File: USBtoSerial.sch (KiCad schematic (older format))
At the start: 8 parts, among them J7 USB_B_Micro, U3 FT231XS

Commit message: change USB to Serial chip, support charging
* exchanges FTDI FT231X for SILabs CP2102N
* adds MicroChip MCP73123 for LiFePO4 charging
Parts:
- removed C10: 100nF, Capacitor_SMD:C_0805_2012Metric, symbol Device:C
- added C?: 4.7μF, Capacitor_SMD:C_0805_2012Metric, symbol Device:C
- added D?: TX, symbol Device:LED
- added D?: RX, symbol Device:LED
- added R?: 47k5, symbol Device:R
- added R?: 22k1, symbol Device:R
- added R?: 1k, symbol Device:R
- added R? (x2): R, symbol Device:R
- C7: value 10nF -> 100nF
- U3: value FT231XS -> CP2102N-A01-GQFN28; footprint Package_SO:QSOP-20_3.9x8.7mm_P0.635mm -> Package_DFN_QFN:QFN-28-1EP_5x5mm_P0.5mm_EP3.35x3.35mm; symbol Interface_USB:FT231XS -> Interface_USB:CP2102N-A01-GQFN28
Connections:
- net labels added: CHR0, CHR1, CHREN, GPIO4, GPIO5, GPIO6, RS485_GPIO2, SUSPEND, VDD, ~CTS, ~DCD, ~DSR, ~DTR, ~RI, ~RSTb, ~RTS, ~RXT, ~SUSPENDb, ~TXT, ~WAKEUP_GPIO3
- net labels removed: CBUS0, CBUS1, CBUS2, CBUS3, CTS, DCD, DSR, DTR, RI, RTS
- wire segments 51 -> 70
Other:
- moved on the sheet: C8, C9, J7, R19, R20

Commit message: update drawing to 882a528a10f6fb48f6454efd446c1280f51ad1f8
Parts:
- D2, D3: renamed from D?; footprint (none) -> LED_SMD:LED_0805_2012Metric
- R26, R27, R28, R29, R30: renamed from R?; footprint (none) -> Resistor_SMD:R_0805_2012Metric
- gave numbers to parts that had none: 1
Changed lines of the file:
@@
 	6900 3450 7100 3450
 $Comp
-L Device:R R?
+L Device:R R28
 U 1 1 5EF23249
 P 5150 2450
-F 0 "R?" H 5220 2496 50  0000 L CNN
+F 0 "R28" H 5220 2496 50  0000 L CNN
 F 1 "47k5" H 5220 2405 50  0000 L CNN
-F 2 "" V 5080 2450 50  0001 C CNN
+F 2 "Resistor_SMD:R_0805_2012Metric" V 5080 2450 50  0001 C CNN
 F 3 "~" H 5150 2450 50  0001 C CNN
 	1    5150 2450
@@
 $EndComp
 $Comp
-L Device:R R?
+L Device:R R27
 U 1 1 5EF23E1A
 P 5150 1850
-F 0 "R?" H 5220 1896 50  0000 L CNN
+F 0 "R27" H 5220 1896 50  0000 L CNN
 F 1 "22k1" H 5220 1805 50  0000 L CNN
-F 2 "" V 5080 1850 50  0001 C CNN
+F 2 "Resistor_SMD:R_0805_2012Metric" V 5080 1850 50  0001 C CNN
 F 3 "~" H 5150 1850 50  0001 C CNN
 	1    5150 1850
@@
 P 5150 2800
 AR Path="/5EF27218" Ref="#PWR?"  Part="1"
-AR Path="/5EFCE977/5EF27218" Ref="#PWR?"  Part="1"
-F 0 "#PWR?" H 5150 2550 50  0001 C CNN
+AR Path="/5EFCE977/5EF27218" Ref="#PWR0108"  Part="1"
+F 0 "#PWR0108" H 5150 2550 50  0001 C CNN
 F 1 "GND" H 5155 2627 50  0000 C CNN
 F 2 "" H 5150 2800 50  0001 C CNN
@@
 	5150 1500 5150 1700
 $Comp
-L Device:R R?
+L Device:R R26
 U 1 1 5EF2AEF8
 P 5800 1600
-F 0 "R?" H 5870 1646 50  0000 L CNN
+F 0 "R26" H 5870 1646 50  0000 L CNN
 F 1 "1k" H 5870 1555 50  0000 L CNN
-F 2 "" V 5730 1600 50  0001 C CNN
+F 2 "Resistor_SMD:R_0805_2012Metric" V 5730 1600 50  0001 C CNN
 F 3 "~" H 5800 1600 50  0001 C CNN
 	1    5800 1600
@@
 P 6300 1050
 AR Path="/5EF2E274" Ref="#PWR?"  Part="1"
-AR Path="/5EFCE977/5EF2E274" Ref="#PWR?"  Part="1"
-F 0 "#PWR?" H 6300 900 50  0001 C CNN
+AR Path="/5EFCE977/5EF2E274" Ref="#PWR0109"  Part="1"
+F 0 "#PWR0109" H 6300 900 50  0001 C CNN
 F 1 "VBUS" H 6315 1223 50  0000 C CNN
 F 2 "" H 6300 1050 50  0001 C CNN
@@
 P 1450 1850
 AR Path="/5EF314AF" Ref="C?"  Part="1"
-AR Path="/5EFCE977/5EF314AF" Ref="C?"  Part="1"
-F 0 "C?" H 1565 1896 50  0000 L CNN
+AR Path="/5EFCE977/5EF314AF" Ref="C6"  Part="1"
+F 0 "C6" H 1565 1896 50  0000 L CNN
 F 1 "4.7μF" H 1565 1805 50  0000 L CNN
 F 2 "Capacitor_SMD:C_0805_2012Metric" H 1488 1700 50  0001 C CNN
@@
 P 1450 1600
 AR Path="/5EF314B9" Ref="#PWR?"  Part="1"
-AR Path="/5EFCE977/5EF314B9" Ref="#PWR?"  Part="1"
-F 0 "#PWR?" H 1450 1450 50  0001 C CNN
+AR Path="/5EFCE977/5EF314B9" Ref="#PWR0110"  Part="1"
+F 0 "#PWR0110" H 1450 1450 50  0001 C CNN
 F 1 "VBUS" H 1465 1773 50  0000 C CNN
 F 2 "" H 1450 1600 50  0001 C CNN
@@
 P 1450 2100
 AR Path="/5EF314C3" Ref="#PWR?"  Part="1"
-AR Path="/5EFCE977/5EF314C3" Ref="#PWR?"  Part="1"
-F 0 "#PWR?" H 1450 1850 50  0001 C CNN
+AR Path="/5EFCE977/5EF314C3" Ref="#PWR0111"  Part="1"
+F 0 "#PWR0111" H 1450 1850 50  0001 C CNN
 F 1 "GND" H 1455 1927 50  0000 C CNN
 F 2 "" H 1450 2100 50  0001 C CNN
@@
 	6900 2750 7100 2750
 $Comp
-L Device:LED D?
+L Device:LED D2
 U 1 1 5EF67E52
 P 1450 3050
-F 0 "D?" H 1443 3267 50  0000 C CNN
+F 0 "D2" H 1443 3267 50  0000 C CNN
 F 1 "TX" H 1443 3176 50  0000 C CNN
-F 2 "" H 1450 3050 50  0001 C CNN
+F 2 "LED_SMD:LED_0805_2012Metric" H 1450 3050 50  0001 C CNN
 F 3 "~" H 1450 3050 50  0001 C CNN
 	1    1450 3050
@@
 ~TXT
 $Comp
-L Device:LED D?
+L Device:LED D3
 U 1 1 5EF69A52
 P 1450 3300
-F 0 "D?" H 1443 3137 50  0000 C CNN
+F 0 "D3" H 1443 3137 50  0000 C CNN
 F 1 "RX" H 1443 3046 50  0000 C CNN
-F 2 "" H 1450 3300 50  0001 C CNN
+F 2 "LED_SMD:LED_0805_2012Metric" H 1450 3300 50  0001 C CNN
 F 3 "~" H 1450 3300 50  0001 C CNN
 	1    1450 3300
@@
 	1150 3300 1300 3300
 $Comp
-L Device:R R?
+L Device:R R29
 U 1 1 5EF6C431
 P 1900 3050
-F 0 "R?" V 1693 3050 50  0000 C CNN
+F 0 "R29" V 1693 3050 50  0000 C CNN
 F 1 "R" V 1784 3050 50  0000 C CNN
-F 2 "" V 1830 3050 50  0001 C CNN
+F 2 "Resistor_SMD:R_0805_2012Metric" V 1830 3050 50  0001 C CNN
 F 3 "~" H 1900 3050 50  0001 C CNN
 	1    1900 3050
@@
 $EndComp
 $Comp
-L Device:R R?
+L Device:R R30
 U 1 1 5EF6CF1D
 P 1900 3300
-F 0 "R?" V 2015 3300 50  0000 C CNN
+F 0 "R30" V 2015 3300 50  0000 C CNN
 F 1 "R" V 2106 3300 50  0000 C CNN
-F 2 "" V 1830 3300 50  0001 C CNN
+F 2 "Resistor_SMD:R_0805_2012Metric" V 1830 3300 50  0001 C CNN
 F 3 "~" H 1900 3300 50  0001 C CNN
 	1    1900 3300

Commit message: Add JCLPCB/LCSC part numbers
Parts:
- C6: LCSC (none) -> C1779
- C7: LCSC (none) -> C49678
- C8, C9: LCSC (none) -> C14857
- D2: LCSC (none) -> C84256
- D3: LCSC (none) -> C2297
- R19, R20: LCSC (none) -> C17594
- R26: LCSC (none) -> C17513
- R27: LCSC (none) -> C17518
- R28: LCSC (none) -> C26011
- R29, R30: LCSC (none) -> C17630
- U3: LCSC (none) -> C105167
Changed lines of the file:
@@
 EESchema Schematic File Version 4
+LIBS:ULPSoilMonitor-cache
 EELAYER 30 0
 EELAYER END
@@
 F 2 "Resistor_SMD:R_0805_2012Metric" V 3930 1900 50  0001 C CNN
 F 3 "~" H 4000 1900 50  0001 C CNN
+F 4 "C17594" H 4000 1900 50  0001 C CNN "LCSC"
 	1    4000 1900
 	0    1    1    0
@@
 F 2 "Resistor_SMD:R_0805_2012Metric" V 3930 1800 50  0001 C CNN
 F 3 "~" H 4000 1800 50  0001 C CNN
+F 4 "C17594" H 4000 1800 50  0001 C CNN "LCSC"
 	1    4000 1800
 	0    -1   -1   0
@@
 F 2 "Capacitor_SMD:C_0805_2012Metric" H 3688 2100 50  0001 C CNN
 F 3 "~" H 3650 2250 50  0001 C CNN
+F 4 "C14857" H 3650 2250 50  0001 C CNN "LCSC"
 	1    3650 2250
 	1    0    0    -1
@@
 F 2 "Capacitor_SMD:C_0805_2012Metric" H 3388 2100 50  0001 C CNN
 F 3 "~" H 3350 2250 50  0001 C CNN
+F 4 "C14857" H 3350 2250 50  0001 C CNN "LCSC"
 	1    3350 2250
 	1    0    0    -1
@@
 F 2 "Capacitor_SMD:C_0805_2012Metric" H 1938 1700 50  0001 C CNN
 F 3 "~" H 1900 1850 50  0001 C CNN
+F 4 "C49678" H 1900 1850 50  0001 C CNN "LCSC"
 	1    1900 1850
 	1    0    0    -1
@@
 F 2 "Package_DFN_QFN:QFN-28-1EP_5x5mm_P0.5mm_EP3.35x3.35mm" H 6850 1650 50  0001 L CNN
 F 3 "https://www.silabs.com/documents/public/data-sheets/cp2102n-datasheet.pdf" H 6450 2100 50  0001 C CNN
+F 4 "C105167" H 6400 2850 50  0001 C CNN "LCSC"
 	1    6400 2850
 	1    0    0    -1
@@
 F 2 "Resistor_SMD:R_0805_2012Metric" V 5080 2450 50  0001 C CNN
 F 3 "~" H 5150 2450 50  0001 C CNN
+F 4 "C26011" H 5150 2450 50  0001 C CNN "LCSC"
 	1    5150 2450
 	1    0    0    -1
@@
 F 2 "Resistor_SMD:R_0805_2012Metric" V 5080 1850 50  0001 C CNN
 F 3 "~" H 5150 1850 50  0001 C CNN
+F 4 "C17518" H 5150 1850 50  0001 C CNN "LCSC"
 	1    5150 1850
 	1    0    0    -1
@@
 F 2 "Resistor_SMD:R_0805_2012Metric" V 5730 1600 50  0001 C CNN
 F 3 "~" H 5800 1600 50  0001 C CNN
+F 4 "C17513" H 5800 1600 50  0001 C CNN "LCSC"
 	1    5800 1600
 	1    0    0    -1
@@
 F 2 "Capacitor_SMD:C_0805_2012Metric" H 1488 1700 50  0001 C CNN
 F 3 "~" H 1450 1850 50  0001 C CNN
+F 4 "C1779" H 1450 1850 50  0001 C CNN "LCSC"
 	1    1450 1850
 	1    0    0    -1
@@
 F 2 "LED_SMD:LED_0805_2012Metric" H 1450 3050 50  0001 C CNN
 F 3 "~" H 1450 3050 50  0001 C CNN
+F 4 "C84256" H 1450 3050 50  0001 C CNN "LCSC"
 	1    1450 3050
 	1    0    0    -1
@@
 F 2 "LED_SMD:LED_0805_2012Metric" H 1450 3300 50  0001 C CNN
 F 3 "~" H 1450 3300 50  0001 C CNN
+F 4 "C2297" H 1450 3300 50  0001 C CNN "LCSC"
 	1    1450 3300
 	1    0    0    -1
@@
 F 2 "Resistor_SMD:R_0805_2012Metric" V 1830 3050 50  0001 C CNN
 F 3 "~" H 1900 3050 50  0001 C CNN
+F 4 "C17630" H 1900 3050 50  0001 C CNN "LCSC"
 	1    1900 3050
 	0    1    1    0
@@
 F 2 "Resistor_SMD:R_0805_2012Metric" V 1830 3300 50  0001 C CNN
 F 3 "~" H 1900 3300 50  0001 C CNN
+F 4 "C17630" H 1900 3300 50  0001 C CNN "LCSC"
 	1    1900 3300
 	0    1    1    0

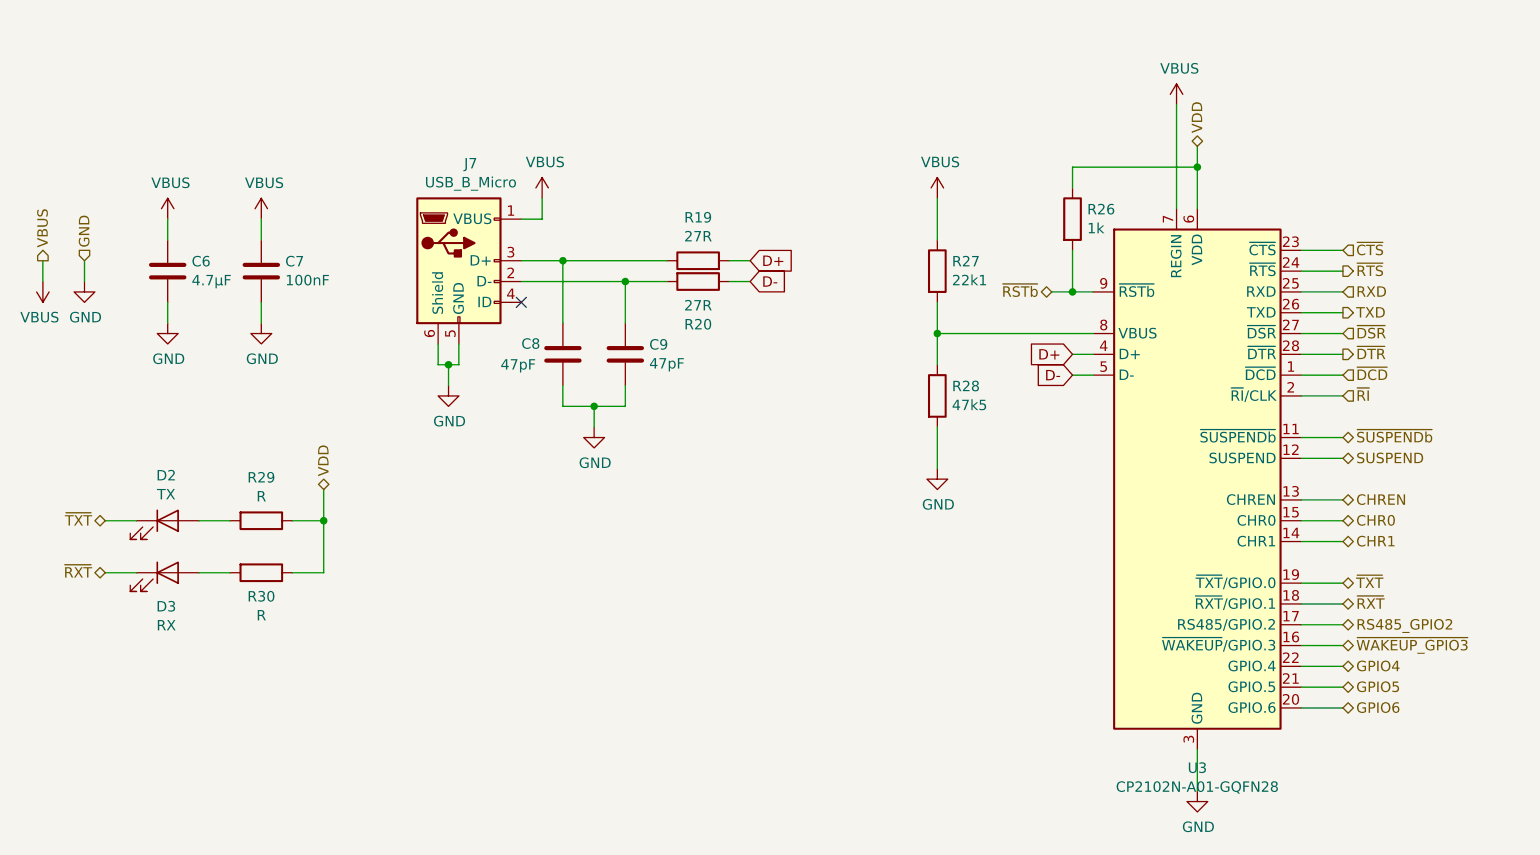
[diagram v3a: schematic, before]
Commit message: Set USB-serial DNP
Disable USB-serial
Add switches for LiFePo charger PROG setting
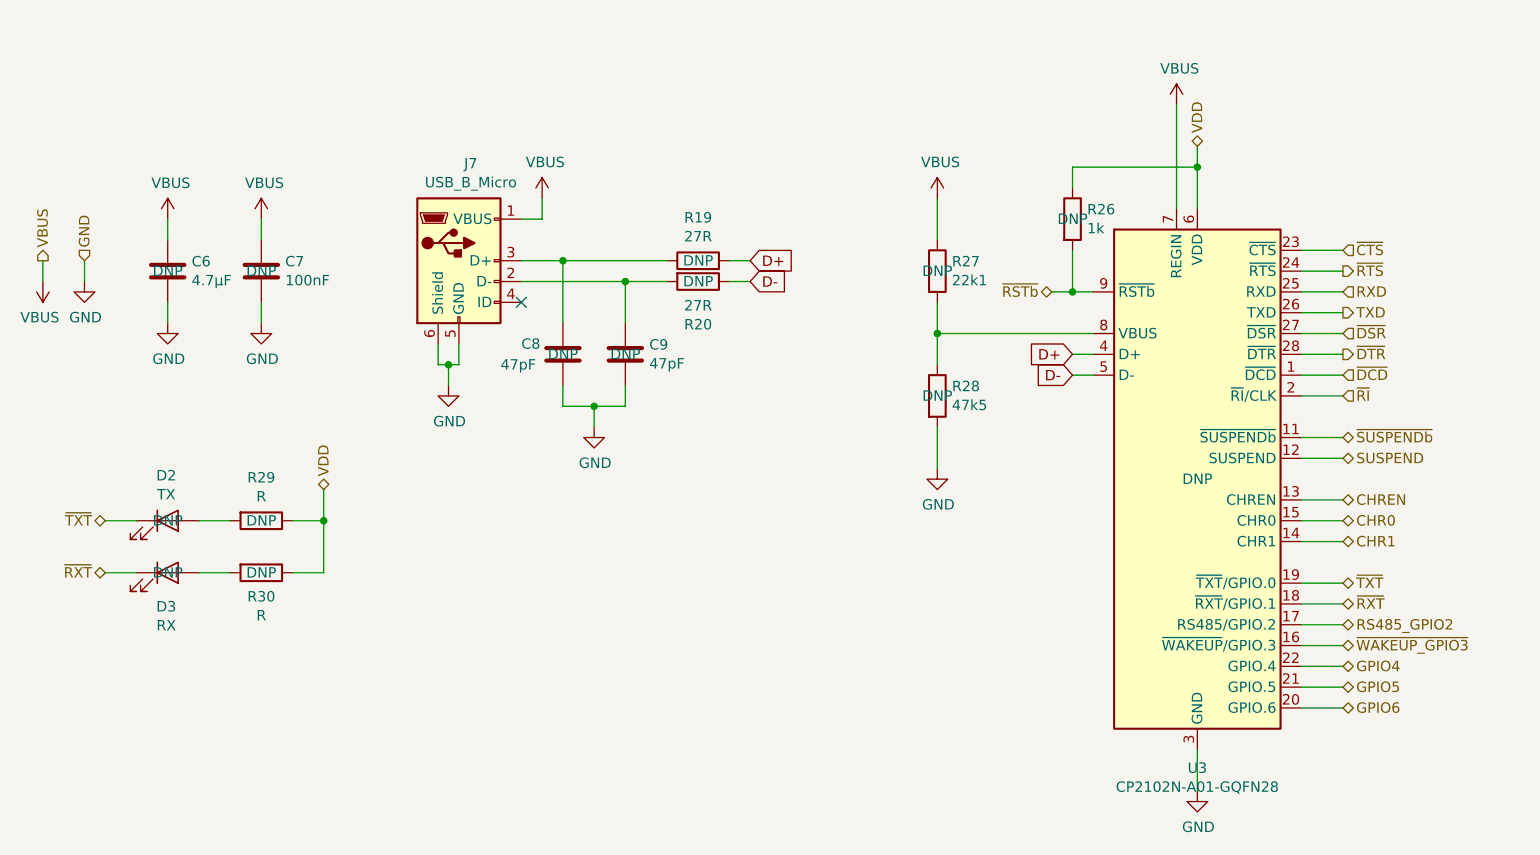
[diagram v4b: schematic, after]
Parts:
- C6, C7, C8, C9, D2, D3, R19, R20, R26, R27, R28, R29, R30, U3: DNP (none) -> DNP
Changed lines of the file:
@@
 F 3 "~" H 4000 1900 50  0001 C CNN
 F 4 "C17594" H 4000 1900 50  0001 C CNN "LCSC"
+F 5 "DNP" V 4000 1900 50  0000 C CNN "DNP"
 	1    4000 1900
 	0    1    1    0
@@
 F 3 "~" H 4000 1800 50  0001 C CNN
 F 4 "C17594" H 4000 1800 50  0001 C CNN "LCSC"
+F 5 "DNP" V 4000 1800 50  0000 C CNN "DNP"
 	1    4000 1800
 	0    -1   -1   0
@@
 F 3 "~" H 3650 2250 50  0001 C CNN
 F 4 "C14857" H 3650 2250 50  0001 C CNN "LCSC"
+F 5 "DNP" H 3650 2250 50  0000 C CNN "DNP"
 	1    3650 2250
 	1    0    0    -1
@@
 F 3 "~" H 3350 2250 50  0001 C CNN
 F 4 "C14857" H 3350 2250 50  0001 C CNN "LCSC"
+F 5 "DNP" H 3350 2250 50  0000 C CNN "DNP"
 	1    3350 2250
 	1    0    0    -1
@@
 F 3 "~" H 1900 1850 50  0001 C CNN
 F 4 "C49678" H 1900 1850 50  0001 C CNN "LCSC"
+F 5 "DNP" H 1900 1850 50  0000 C CNN "DNP"
 	1    1900 1850
 	1    0    0    -1
@@
 F 3 "https://www.silabs.com/documents/public/data-sheets/cp2102n-datasheet.pdf" H 6450 2100 50  0001 C CNN
 F 4 "C105167" H 6400 2850 50  0001 C CNN "LCSC"
+F 5 "DNP" H 6400 2850 50  0000 C CNN "DNP"
 	1    6400 2850
 	1    0    0    -1
@@
 F 3 "~" H 5150 2450 50  0001 C CNN
 F 4 "C26011" H 5150 2450 50  0001 C CNN "LCSC"
+F 5 "DNP" H 5150 2450 50  0000 C CNN "DNP"
 	1    5150 2450
 	1    0    0    -1
@@
 F 3 "~" H 5150 1850 50  0001 C CNN
 F 4 "C17518" H 5150 1850 50  0001 C CNN "LCSC"
+F 5 "DNP" H 5150 1850 50  0000 C CNN "DNP"
 	1    5150 1850
 	1    0    0    -1
@@
 F 3 "~" H 5800 1600 50  0001 C CNN
 F 4 "C17513" H 5800 1600 50  0001 C CNN "LCSC"
+F 5 "DNP" H 5800 1600 50  0000 C CNN "DNP"
 	1    5800 1600
 	1    0    0    -1
@@
 F 3 "~" H 1450 1850 50  0001 C CNN
 F 4 "C1779" H 1450 1850 50  0001 C CNN "LCSC"
+F 5 "DNP" H 1450 1850 50  0000 C CNN "DNP"
 	1    1450 1850
 	1    0    0    -1
@@
 F 3 "~" H 1450 3050 50  0001 C CNN
 F 4 "C84256" H 1450 3050 50  0001 C CNN "LCSC"
+F 5 "DNP" H 1450 3050 50  0000 C CNN "DNP"
 	1    1450 3050
 	1    0    0    -1
@@
 F 3 "~" H 1450 3300 50  0001 C CNN
 F 4 "C2297" H 1450 3300 50  0001 C CNN "LCSC"
+F 5 "DNP" H 1450 3300 50  0000 C CNN "DNP"
 	1    1450 3300
 	1    0    0    -1
@@
 F 3 "~" H 1900 3050 50  0001 C CNN
 F 4 "C17630" H 1900 3050 50  0001 C CNN "LCSC"
+F 5 "DNP" V 1900 3050 50  0000 C CNN "DNP"
 	1    1900 3050
 	0    1    1    0
@@
 F 3 "~" H 1900 3300 50  0001 C CNN
 F 4 "C17630" H 1900 3300 50  0001 C CNN "LCSC"
+F 5 "DNP" V 1900 3300 50  0000 C CNN "DNP"
 	1    1900 3300
 	0    1    1    0

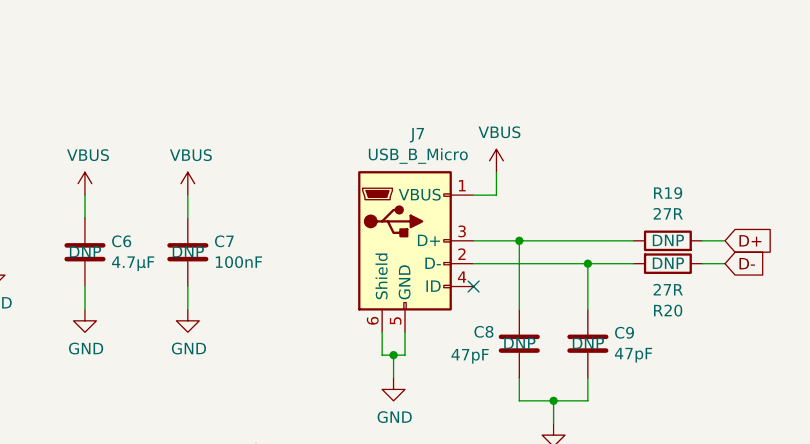
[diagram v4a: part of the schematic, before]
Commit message: DNP micro-usb
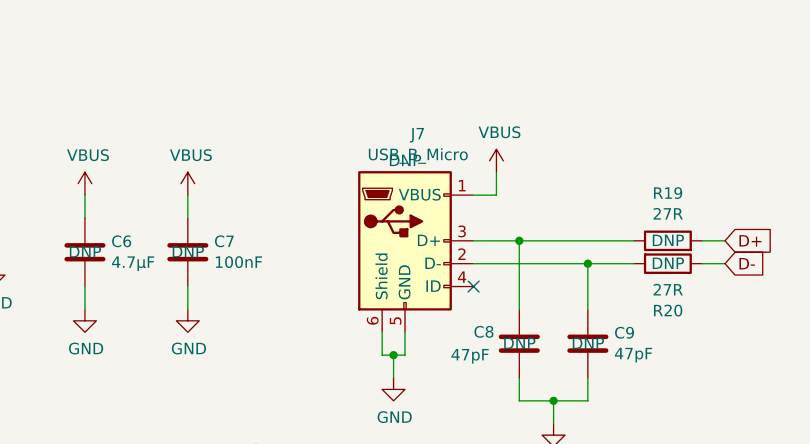
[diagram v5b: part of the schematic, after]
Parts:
- J7: DNP (none) -> DNP
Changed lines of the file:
@@
 F 2 "Connector_USB:USB_Micro-B_Amphenol_10103594-0001LF_Horizontal" H 3000 1750 50  0001 C CNN
 F 3 "~" H 3000 1750 50  0001 C CNN
+F 4 "DNP" H 2850 2150 50  0000 C CNN "DNP"
 	1    2850 1800
 	1    0    0    -1

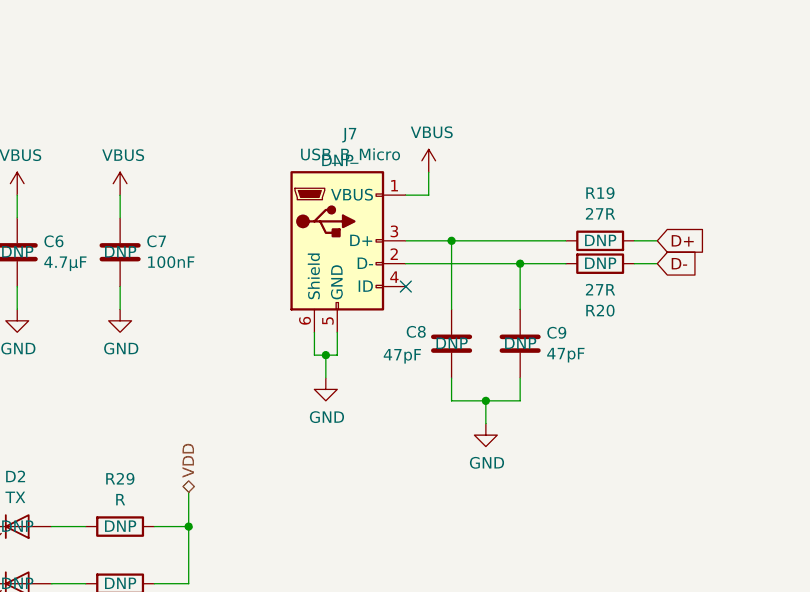
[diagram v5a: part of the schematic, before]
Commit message: Remove USB-mini connector
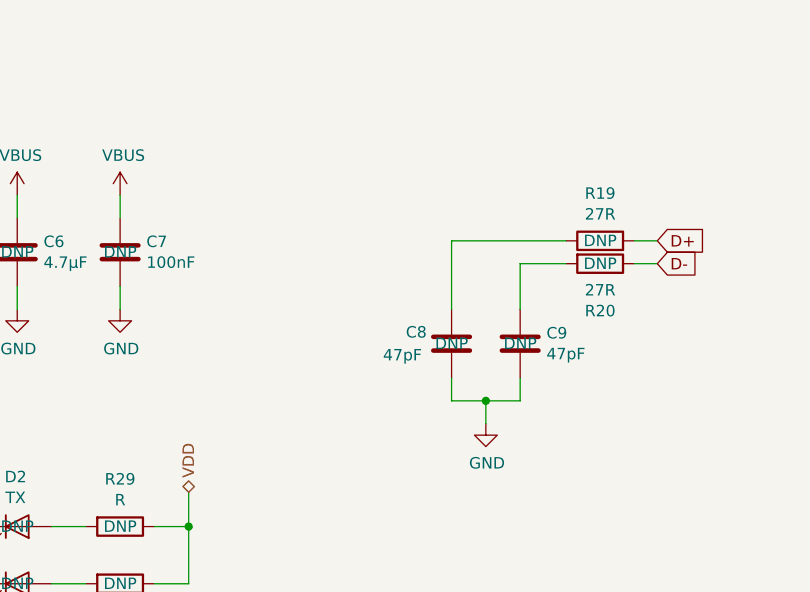
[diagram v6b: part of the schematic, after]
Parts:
- removed J7: USB_B_Micro, Connector_USB:USB_Micro-B_Amphenol_10103594-0001LF_Horizontal, symbol Connector:USB_B_Micro
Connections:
- no-connect marks 1 -> 0
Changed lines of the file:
@@
 $EndDescr
-$Comp
-L Connector:USB_B_Micro J?
-U 1 1 5EFD2D90
-P 2850 1800
-AR Path="/5EFD2D90" Ref="J?"  Part="1"
-AR Path="/5EFCE977/5EFD2D90" Ref="J7"  Part="1"
-F 0 "J7" H 2907 2267 50  0000 C CNN
-F 1 "USB_B_Micro" H 2907 2176 50  0000 C CNN
-F 2 "Connector_USB:USB_Micro-B_Amphenol_10103594-0001LF_Horizontal" H 3000 1750 50  0001 C CNN
-F 3 "~" H 3000 1750 50  0001 C CNN
-F 4 "DNP" H 2850 2150 50  0000 C CNN "DNP"
-	1    2850 1800
-	1    0    0    -1
-$EndComp
-$Comp
-L power:VBUS #PWR?
-U 1 1 5EFD2D96
-P 3250 1500
-AR Path="/5EFD2D96" Ref="#PWR?"  Part="1"
-AR Path="/5EFCE977/5EFD2D96" Ref="#PWR040"  Part="1"
-F 0 "#PWR040" H 3250 1350 50  0001 C CNN
-F 1 "VBUS" H 3265 1673 50  0000 C CNN
-F 2 "" H 3250 1500 50  0001 C CNN
-F 3 "" H 3250 1500 50  0001 C CNN
-	1    3250 1500
-	1    0    0    -1
-$EndComp
-Wire Wire Line
-	3150 1600 3250 1600
-Wire Wire Line
-	3250 1600 3250 1500
-Wire Wire Line
-	2750 2200 2750 2300
-Wire Wire Line
-	2750 2300 2800 2300
-Wire Wire Line
-	2850 2300 2850 2200
-$Comp
-L power:GND #PWR?
-U 1 1 5EFD2DA3
-P 2800 2400
-AR Path="/5EFD2DA3" Ref="#PWR?"  Part="1"
-AR Path="/5EFCE977/5EFD2DA3" Ref="#PWR045"  Part="1"
-F 0 "#PWR045" H 2800 2150 50  0001 C CNN
-F 1 "GND" H 2805 2227 50  0000 C CNN
-F 2 "" H 2800 2400 50  0001 C CNN
-F 3 "" H 2800 2400 50  0001 C CNN
-	1    2800 2400
-	1    0    0    -1
-$EndComp
-Wire Wire Line
-	2800 2400 2800 2300
-Connection ~ 2800 2300
-Wire Wire Line
-	2800 2300 2850 2300
 $Comp
 L Device:R R?
@@
 $EndComp
 Wire Wire Line
-	3150 1800 3350 1800
-Wire Wire Line
 	3850 1900 3650 1900
 Wire Wire Line
@@
 Wire Wire Line
 	4250 1900 4150 1900
-NoConn ~ 3150 2000
 $Comp
 L Device:C C?
@@
 Wire Wire Line
 	3350 1800 3350 2100
-Connection ~ 3350 1800
 Wire Wire Line
 	3350 1800 3850 1800
 Wire Wire Line
 	3650 1900 3650 2100
-Connection ~ 3650 1900
-Wire Wire Line
-	3650 1900 3150 1900
 $Comp
 L Device:C C?
